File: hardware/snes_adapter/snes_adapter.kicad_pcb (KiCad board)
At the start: 2 copper layers, 97.8 x 27.9 mm, 4 parts, among them J1 CART SLOT TOP ROW, J2 CART SLOT BOTTOM ROW, J3 SNES_Slot

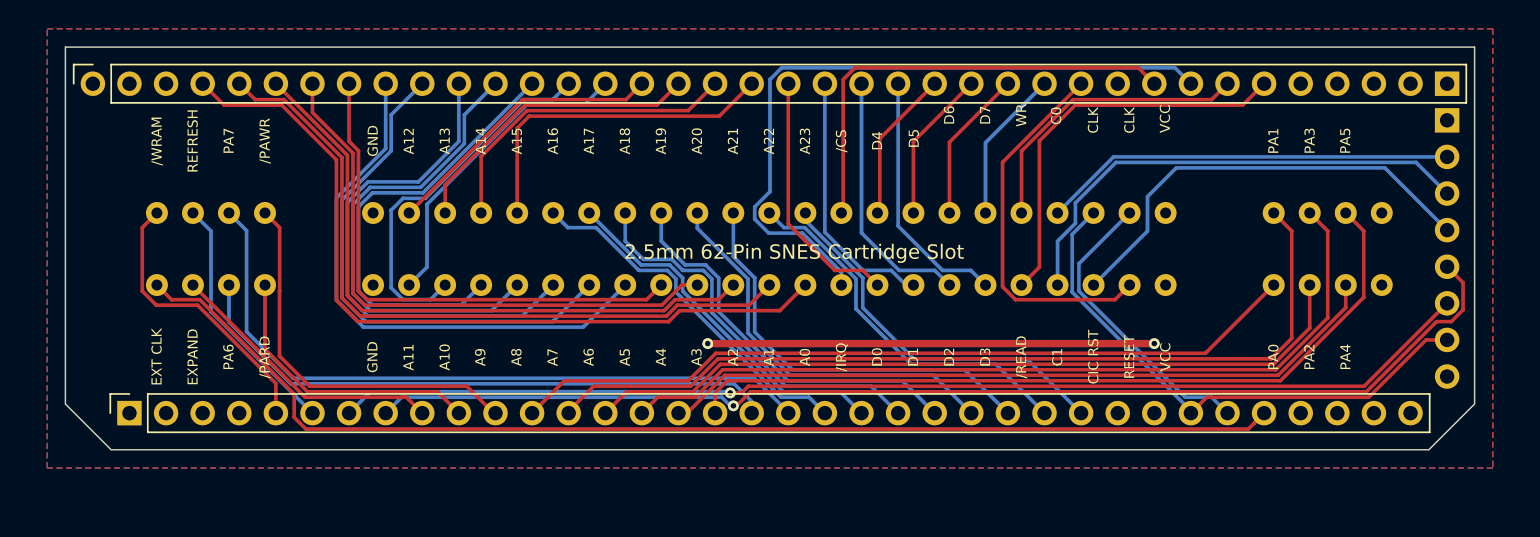
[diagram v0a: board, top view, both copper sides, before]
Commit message: Move cic uc to SNES breakout board and update
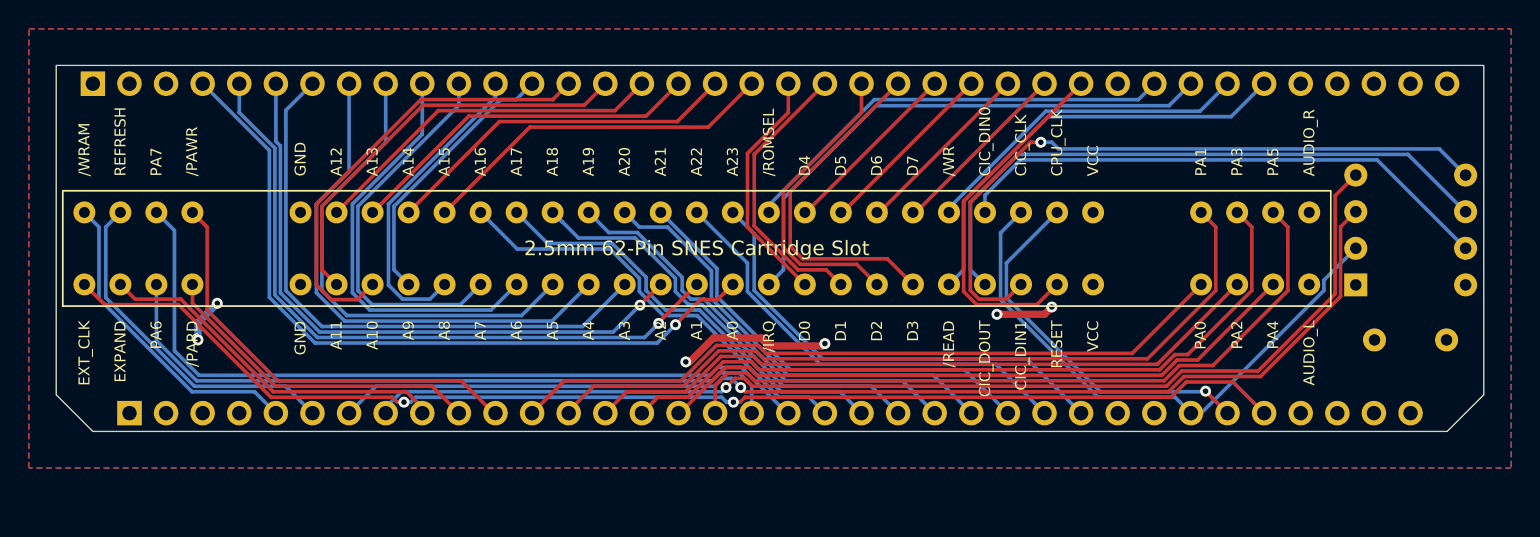
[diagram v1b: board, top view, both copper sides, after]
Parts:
- removed JCIC1: CIC_HEADER, Connector_PinHeader_2.54mm:PinHeader_1x08_P2.54mm_Vertical
- added C1: 0.1 uF, Capacitor_THT:C_Disc_D5.0mm_W2.5mm_P5.00mm, B.Cu at (191.8, 94.0)
- added U1: PIC12F629-IP, Package_DIP:DIP-8_W7.62mm, B.Cu at (190.5, 90.2)
- J1: footprint Connector_PinSocket_2.54mm:PinSocket_1x38_P2.54mm_Vertical -> Connector_PinHeader_2.54mm:PinHeader_1x38_P2.54mm_Vertical; moved to B.Cu
- J2: footprint Connector_PinSocket_2.54mm:PinSocket_1x36_P2.54mm_Vertical -> Connector_PinHeader_2.54mm:PinHeader_1x36_P2.54mm_Vertical; moved to B.Cu
- J3: footprint !sanni:SNES Slot -> !OSCR:SNES Slot
- moved J3 37.6 mm to (144.8, 87.6)
- turned J1 to -90 degrees
- turned J2 to -90 degrees
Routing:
- net VCC: track 31.0 -> 14.7 mm, vias 2 -> 4
- net CIC RESET: track 31.1 -> 47.3 mm, vias 0 -> 1
- net A9: track 30.9 -> 19.0 mm
- net A8: track 33.3 -> 21.8 mm
- net D7: track 48.6 -> 38.0 mm
- net CIC DATA 1: track 34.1 -> 43.5 mm
- net CIC DATA 0: track 28.6 -> 38.1 mm
- net A7: track 35.7 -> 26.8 mm
- net A11: track 22.0 -> 29.1 mm
- net D28: track 41.9 -> 48.9 mm
- net A6: track 36.1 -> 29.1 mm
- net D23: track 61.6 -> 54.8 mm
- net D3: track 17.3 -> 24.0 mm
- net D34: track 17.6 -> 24.0 mm
- net D24: track 54.3 -> 48.0 mm
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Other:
- board size 97.8 x 27.9 mm -> 99.1 x 25.4 mm
- board text removed: "/CS"
- board text removed: "/IRQ"
- board text removed: "/PARD"
- board text removed: "/PAWR"
- board text removed: "/READ"
- board text removed: "/WRAM"
- board text removed: "2.5mm 62-Pin SNES Cartridge Slot"
- board text removed: "A16"
- board text removed: "A17"
- board text removed: "A18"
- board text removed: "A19"
- board text removed: "A20"
- board text removed: "A21"
- board text removed: "A22"
- board text removed: "A23"
- board text removed: "C0"
- board text removed: "C1"
- board text removed: "CIC RST"
- board text removed: "CLK"
- board text removed: "CR"
- board text removed: "EXPAND"
- board text removed: "EXT CLK"
- board text removed: "PA0"
- board text removed: "PA1"
- board text removed: "PA2"
- board text removed: "PA3"
- board text removed: "PA4"
- board text removed: "PA5"
- board text removed: "PA6"
- board text removed: "PA7"
- board text removed: "REFRESH"
- board text removed: "RESET"
- board text removed: "WR"

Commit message: move SNES updates to clean branch
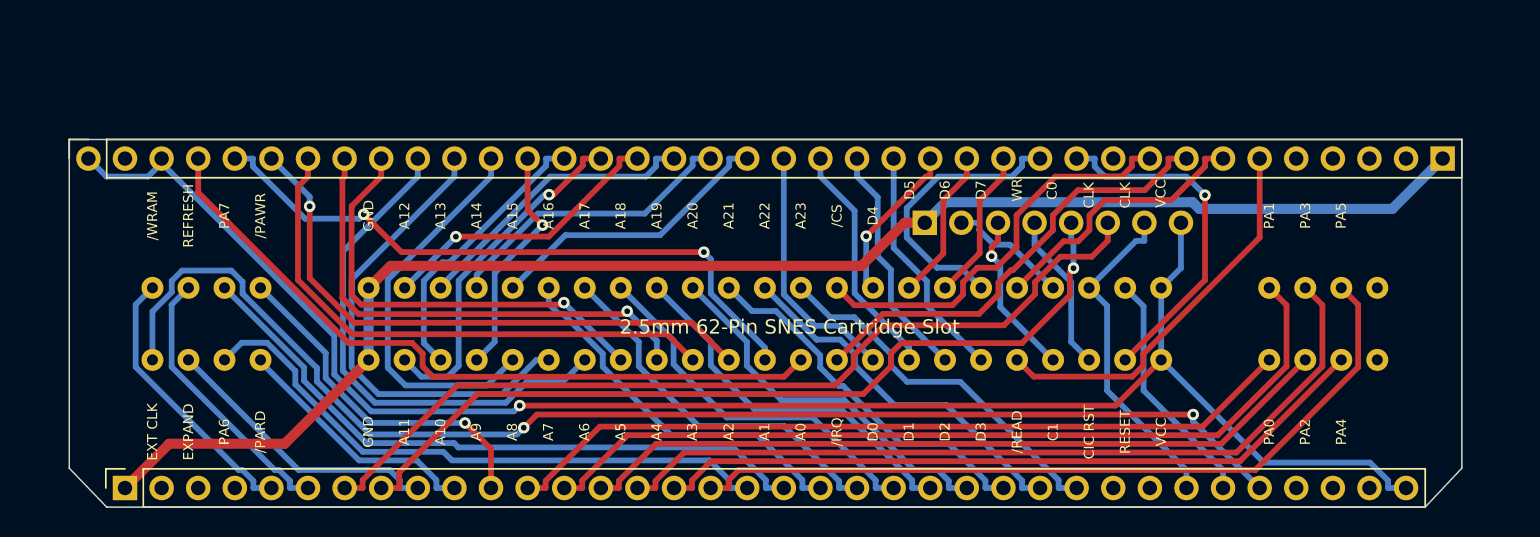
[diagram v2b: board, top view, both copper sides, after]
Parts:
- removed C1: 0.1 uF, Capacitor_THT:C_Disc_D5.0mm_W2.5mm_P5.00mm
- removed U1: PIC12F629-IP, Package_DIP:DIP-8_W7.62mm
- added JCIC1: Conn_01x08, Connector_PinHeader_2.54mm:PinHeader_1x08_P2.54mm_Vertical, B.Cu at (178.4, 85.8)
- J1: footprint Connector_PinHeader_2.54mm:PinHeader_1x38_P2.54mm_Vertical -> Connector_PinSocket_2.54mm:PinSocket_1x38_P2.54mm_Vertical; moved to F.Cu
- J2: footprint Connector_PinHeader_2.54mm:PinHeader_1x36_P2.54mm_Vertical -> Connector_PinSocket_2.54mm:PinSocket_1x36_P2.54mm_Vertical; moved to F.Cu
- J3: footprint !OSCR:SNES Slot -> !sanni:SNES Slot
- moved J3 38.6 mm to (107.0, 95.4)
- moved J1 5.20 mm to (102.6, 81.4), turned to 90 degrees
- moved J2 5.20 mm to (105.1, 104.3), turned to 90 degrees
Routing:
- net VCC: track 14.7 -> 116.9 mm, vias 4 -> 1
- net GND: track 3.09 -> 104.2 mm, vias 2 -> 0
- net CIC RESET: track 47.3 -> 11.1 mm, vias 1 -> 0
- net CIC DATA 1: track 43.5 -> 11.5 mm, vias 0 -> 1
- net CIC DATA 0: track 38.1 -> 8.54 mm
- net D40: track 78.8 -> 59.7 mm
- net D41: track 79.2 -> 62.6 mm, vias 1 -> 0
- net CLK2: track 39.7 -> 23.1 mm
- net A10: track 31.3 -> 19.5 mm
- net D29: track 55.0 -> 45.4 mm
- net CLK1: track 26.1 -> 16.7 mm, vias 1 -> 0
- net D34: track 24.0 -> 16.5 mm
- net D28: track 48.9 -> 41.8 mm
- net D30: track 12.8 -> 19.6 mm
- net A6: track 29.1 -> 35.8 mm
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- removed copper zone on F.Cu, net GND
- removed copper zone on B.Cu, net VCC
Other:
- board size 99.1 x 25.4 mm -> 96.6 x 25.5 mm
- board text added: "/CS"
- board text added: "/IRQ"
- board text added: "/PARD"
- board text added: "/PAWR"
- board text added: "/READ"
- board text added: "/WRAM"
- board text added: "2.5mm 62-Pin SNES Cartridge Slot"
- board text added: "A16"
- board text added: "A17"
- board text added: "A18"
- board text added: "A19"
- board text added: "A20"
- board text added: "A21"
- board text added: "A22"
- board text added: "A23"
- board text added: "C0"
- board text added: "C1"
- board text added: "CIC RST"
- board text added: "CLK"
- board text added: "CR"
- board text added: "EXPAND"
- board text added: "EXT CLK"
- board text added: "PA0"
- board text added: "PA1"
- board text added: "PA2"
- board text added: "PA3"
- board text added: "PA4"
- board text added: "PA5"
- board text added: "PA6"
- board text added: "PA7"
- board text added: "REFRESH"
- board text added: "RESET"
- board text added: "WR"
- board text removed: "3v3"
- board text removed: "MISO"
- board text removed: "MOSI"
- board text removed: "SCK"
- board text removed: "SS"

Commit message: wip; down sizing and re-routing traces
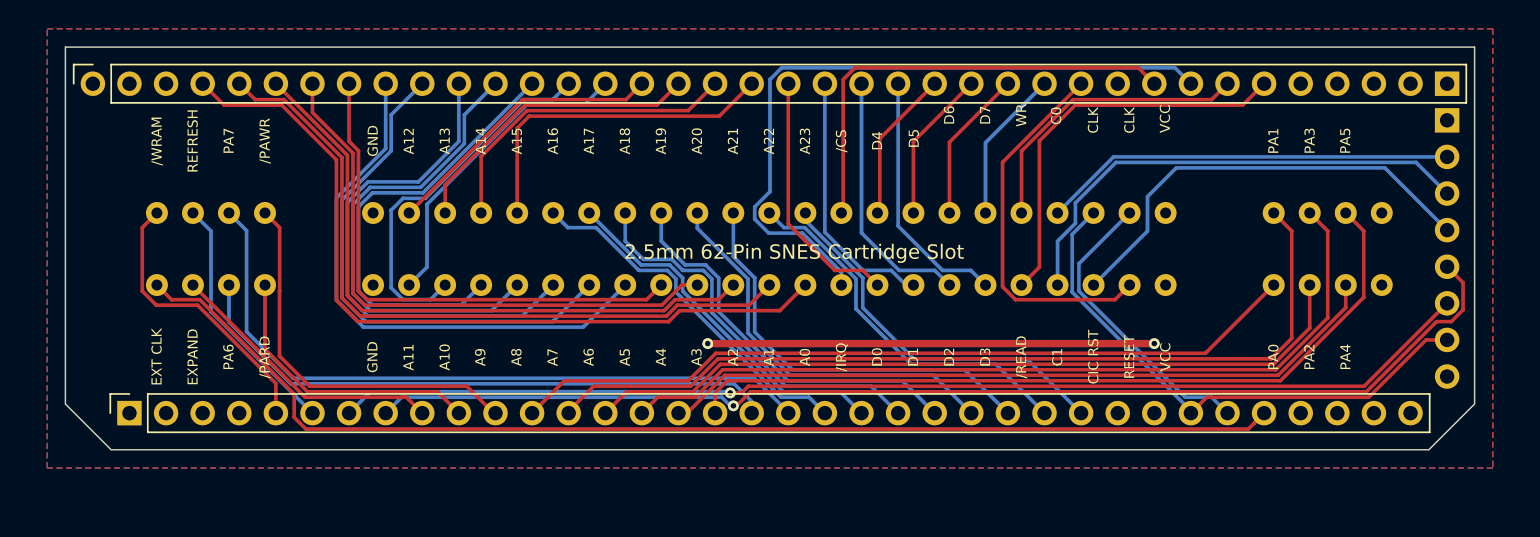
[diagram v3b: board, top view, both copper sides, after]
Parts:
- JCIC1: value Conn_01x08 -> CIC_HEADER
- moved JCIC1 21.3 mm to (196.8, 96.5), turned to 0 degrees
- moved J1 5.20 mm to (102.9, 76.2)
- moved J2 5.20 mm to (105.4, 99.1)
- moved J3 5.20 mm to (107.3, 90.2)
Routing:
- net GND: track 104.2 -> 0.00 mm
- net VCC: track 116.9 -> 31.0 mm, vias 1 -> 2
- net CIC DATA 1: track 11.5 -> 34.1 mm, vias 1 -> 0
- net D40: track 59.7 -> 81.7 mm
- net CIC DATA 0: track 8.54 -> 28.6 mm
- net CIC RESET: track 11.1 -> 31.1 mm
- net D7: track 31.5 -> 48.6 mm
- net D41: track 62.6 -> 79.4 mm, vias 0 -> 1
- net CLK2: track 23.1 -> 37.8 mm
- net A9: track 16.3 -> 30.9 mm, vias 1 -> 0
- net D30: track 19.6 -> 10.7 mm
- net CLK0: track 90.5 -> 82.4 mm, vias 2 -> 0
- net A5: track 31.0 -> 38.5 mm, vias 1 -> 0
- net A10: track 19.5 -> 25.9 mm
- net A8: track 27.4 -> 33.3 mm
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- added copper zone on F.Cu, net GND
- added copper zone on B.Cu, net VCC
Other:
- board size 96.6 x 25.5 mm -> 97.8 x 27.9 mm
- board text added: "3v3"
- board text added: "MISO"
- board text added: "MOSI"
- board text added: "SCK"
- board text added: "SS"
